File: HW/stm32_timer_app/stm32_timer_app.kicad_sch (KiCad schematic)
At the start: 62 parts, among them J1 105164-0001, J2 61300411121, J3 61300411121, J4 691213710002, J5 691213710002, U1 RT9193-33GB, U2 MOC3041SM, U3 STM32F103C8T6, U4 MAX31865 AMPLIFIER, U5 MMBT2222A-7-F, Y1 ABLS-8.000MHZ-B2-T, Y2 ABS25-32.768KHZ-6-4-T

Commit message: schematic
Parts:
- removed R10: 100K, Resistor_SMD:R_0603_1608Metric, symbol Device:R
- removed R11: 330, Resistor_SMD:R_0603_1608Metric, symbol Device:R
- removed S4: MSS6-V-T_R, MSS6-V-T_R:SW_MSS6-V-T_R, symbol MSS6-V-T_R:MSS6-V-T_R
- removed U3: STM32F103C8T6, STM32F103C8T6:QFP50P900X900X160-48N, symbol STM32F103C8T6:STM32F103C8T6
- removed U4: MAX31865 AMPLIFIER, MAX31865:MAX31865, symbol MAX31865:MAX31865 AMPLIFIER
- removed Y1: ABLS-8.000MHZ-B2-T, ABLS-8.000MHZ-B2-T:XTAL_ABLS-8.000MHZ-B2-T, symbol ABLS-8.000MHZ-B2-T:ABLS-8.000MHZ-B2-T
- removed Y2: ABS25-32.768KHZ-6-4-T, ABS25-32.768KHZ-6-4-T:XTAL_ABS25-32.768KHZ-6-4-T, symbol ABS25-32.768KHZ-6-4-T:ABS25-32.768KHZ-6-4-T
- added C16, C17: 105, LD03ZD475MAB2A:CAPC1608X90, symbol LD03ZD475MAB2A:LD03ZD475MAB2A
- added J4, J5: 61300411121, 61300411121:CONN_61300411121_WRE, symbol 61300411121:61300411121
- added LED1, LED2: 150060GS75000, 150060GS75000:LED_150060GS75000_WRE, symbol 150060GS75000:150060GS75000
- added LED3, LED4: 150060GS75000, LED_150060GS75000_WRE, symbol 150060GS75000:150060GS75000
- added R19: 100K, Resistor_SMD:R_0603_1608Metric, symbol Device:R
- added R20, R21, R22, R4, R6, R8, R9: 330, Resistor_SMD:R_0603_1608Metric, symbol Device:R
- added S2, S5: 1571527-1, 1571527-1:SW_1571527-1, symbol 1571527-1:1571527-1
- added S7, S8: MSS-102559-14A-D, MSS-102559-14A-D:SW_MSS-102559-14A-D, symbol MSS-102559-14A-D:MSS-102559-14A-D
- added U2: STM32F103C8T6, STM32F103C8T6:QFP50P900X900X160-48N, symbol STM32F103C8T6:STM32F103C8T6
- added U3: MAX31865 AMPLIFIER, MAX31865:MAX31865, symbol MAX31865:MAX31865 AMPLIFIER
- added Y1: ABM3-8.000MHZ-J4Q-T, ABM3_8_000MHZ_J4Q_T:XTAL_ABM3-8.000MHZ-J4Q-T, symbol ABM3-8.000MHZ-J4Q-T:ABM3-8.000MHZ-J4Q-T
- added Y2: ABS07-32.768KHZ-T, ABS07-32.768KHZ-T:XTAL_ABS07-32.768KHZ-T, symbol ABS07-32.768KHZ-T:ABS07-32.768KHZ-T
- LED5: renamed from LED1; footprint LED_150060GS75000_WRE -> 150060GS75000:LED_150060GS75000_WRE
- LED6: renamed from LED2; footprint LED_150060GS75000_WRE -> 150060GS75000:LED_150060GS75000_WRE
- renumbered C13 to C1, C3 to C10, C4 to C11, C5 to C12, C1 to C13, C2 to C14, C7 to C15, C12 to C2, C6 to C20, C8 to C3, C9 to C4, C16 to C5, C10 to C6, C15 to C7, C14 to C8, C11 to C9, J4 to J1, J3 to J2, J5 to J3, J2 to J6, J1 to J7, MT3 to MT1, R9 to R1, R7 to R10, R8 to R11, R15 to R12, R14 to R13, R13 to R14, R21 to R15, R20 to R16, R19 to R17, R16 to R18, R25 to R2, R12 to R23, R4 to R24, R1 to R25, R2 to R26, R3 to R27, R26 to R3, R29 to R5, R27 to R7, S1 to S4, S2 to S6, U2 to U1, U1 to U4
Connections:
- net +3.3V: now also DS1.2 (VCC), LS1.P, J4.1, J5.1, LED1.2, LED2.2, R20.2, R21.2, R22.2, S7.2, S8.2, U2.24 (VDD), U2.36 (VDD), U2.48 (VDD), U2.9 (VDDA), U3.1 (VIN)
- net BOOT0: now also U2.44 (BOOT0)
- net BOOT1: now also R19.2, U2.20 (PB2)
- net OSCIN: now also U2.5 (PD0_OSC_IN), Y1.1
- net OSCOUT: now also U2.6 (PD1_OSC_OUT), Y1.2
- net PA0: now also U2.10 (PA0_WKUP); no longer MT2.A, R16.1
- net PA1: now also U2.11 (PA1); no longer MT2.B, R15.1
- net PA11: now also U2.32 (PA11)
- net PA12: now also U2.33 (PA12)
- net PA2: now also U2.12 (PA2); no longer MT2.2, R17.1
- net PA3: now also U2.13 (PA3)
- net PA4: now also R22.1, S5.2, S5.4, U2.14 (PA4); no longer S3.2, S3.4
- net PA5: now also DS1.3 (SCK), U2.15 (PA5)
- net PA6: now also DS1.5 (RES), U2.16 (PA6)
- net PA7: now also DS1.4 (SDA), U2.17 (PA7)
- net PB7: now also J4.4, U2.43 (PB7); no longer J2.4, R2.1
- net PC13: now also U2.2 (PC13-TAMPER-RTC)
- net PC14: now also U2.3 (PC14-OSC32_IN), Y2.1
- net PC15: now also U2.4 (PC15-OSC32_OUT), Y2.2
- net RESET: now also U2.7 (NRST)
- net SWDCLK: now also U2.37 (PA14)
- net SWDIO: now also U2.34 (PA13)
- net PB1: now reaches U5.1 (B)
- net PB1: now also U2.19 (PB1)
- net at U5.3 (C): now also LS1.N
- net +3.3VT: now reaches J2.1
- net +3.3VT: now also LED3.2, LED4.2
- net PA10T: now reaches J2.3
- net PA10T: now also R8.1
- net PB3: now reaches DS1.6 (DC)
- net PB3: now also U2.39 (PB3)
- net PB6: now reaches DS1.7 (CS)
- net PB6: now also U2.42 (PB6)
- net at R18.1: now also S7.1
- new net: J2.4, R2.1
- new net: LED1.1, R4.2
- new net: LED2.1, R6.2
- new net: LED4.1, R9.2
- new net: S5.1, S5.3
- new net: R19.1, S8.1
- new net: LED3.1, R8.2
- new net: S2.1, S2.3
- new net: U2.23 (VSS), U2.35 (VSS), U2.47 (VSS), U2.8 (VSSA)
- new net PA10: J4.3, U2.31 (PA10)
- new net PA15: J5.3, U2.38 (PA15)
- new net PA8: C16.1, R20.1, S2.2, S2.4, U2.29 (PA8)
- new net PA9: C17.1, R21.1, S3.2, S3.4, U2.30 (PA9)
- new net PB0: MT2.2, R17.1, U2.18 (PB0)
- new net PB10: J5.4, U2.21 (PB10)
- new net PB11: U2.22 (PB11), U3.8 (RDY)
- new net PB12: U2.25 (PB12), U3.7 (CS)
- new net PB13: U2.26 (PB13), U3.4 (CLK)
- new net PB14: U2.27 (PB14), U3.6 (SDI)
- new net PB15: U2.28 (PB15), U3.5 (SDO)
- new net PB4: MT2.B, R15.1, U2.40 (PB4)
- new net PB5: MT2.A, R16.1, U2.41 (PB5)
- new net PB8: R4.1, U2.45 (PB8)
- new net PB9: R6.1, U2.46 (PB9)
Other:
- note added: "BUZZER"
- note added: "LEFT OVER PINs"
- note added: "MAX31865 AMPLIFIER"
- note added: "TRIAC DRIVE CONNECTOR"
- moved on the sheet: C1, C10, C11, C12, C13, C14, C15, C19, C2, C20, C3, C4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

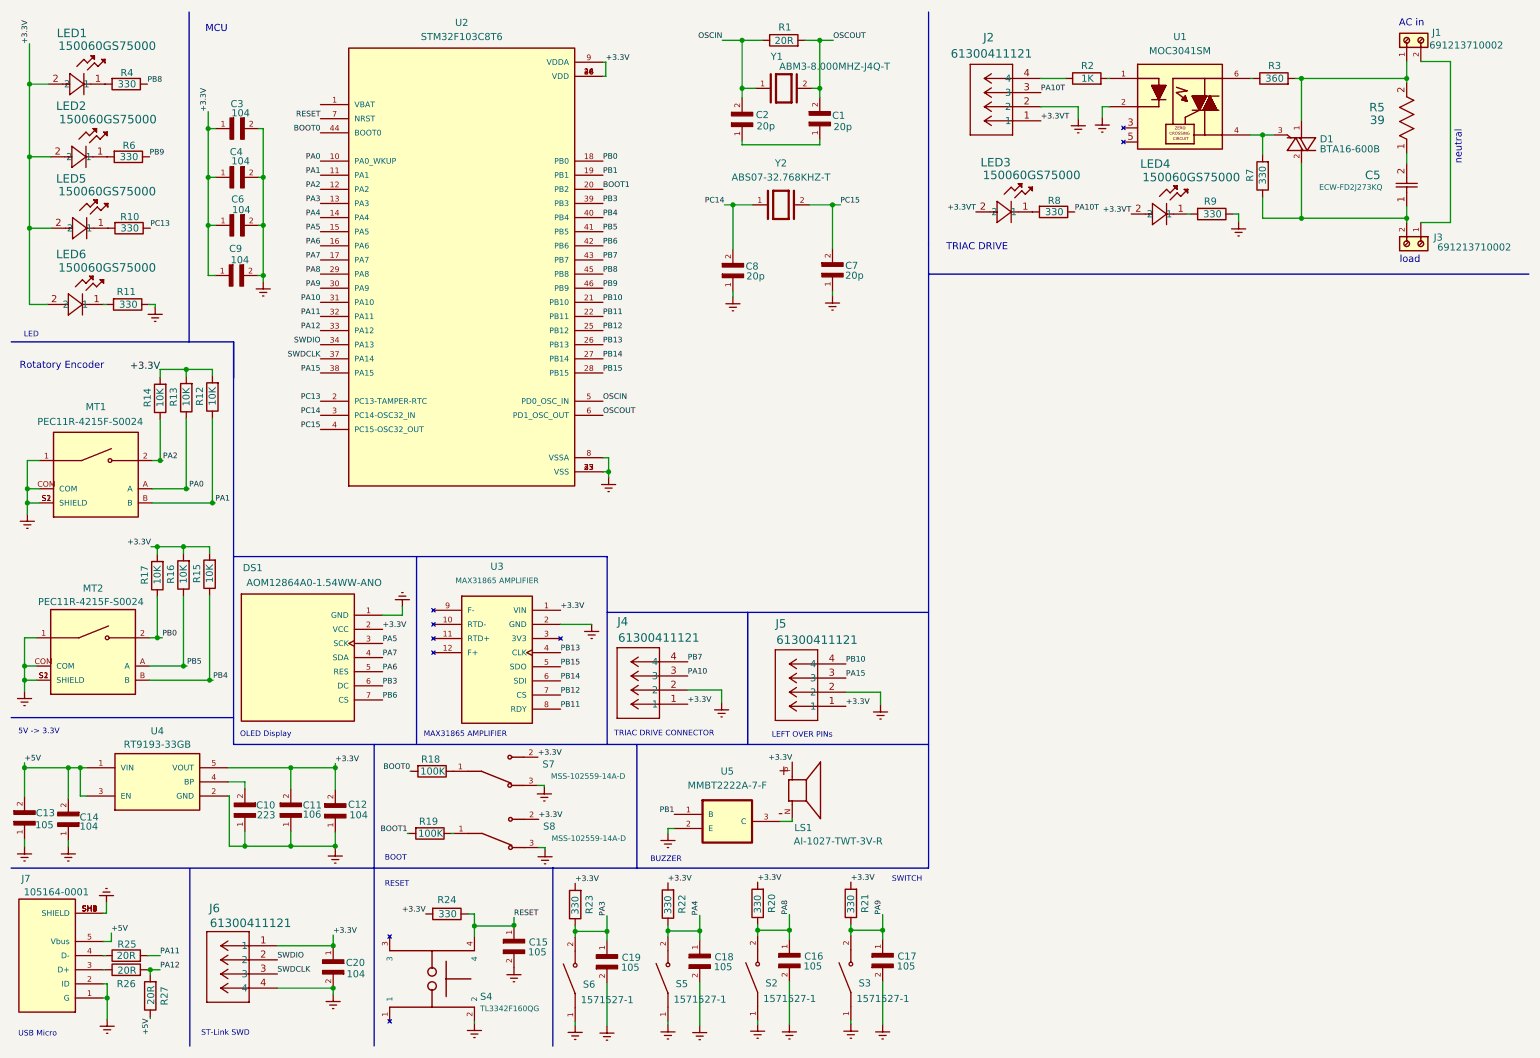
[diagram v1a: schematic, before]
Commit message: schematic update
mcu changed
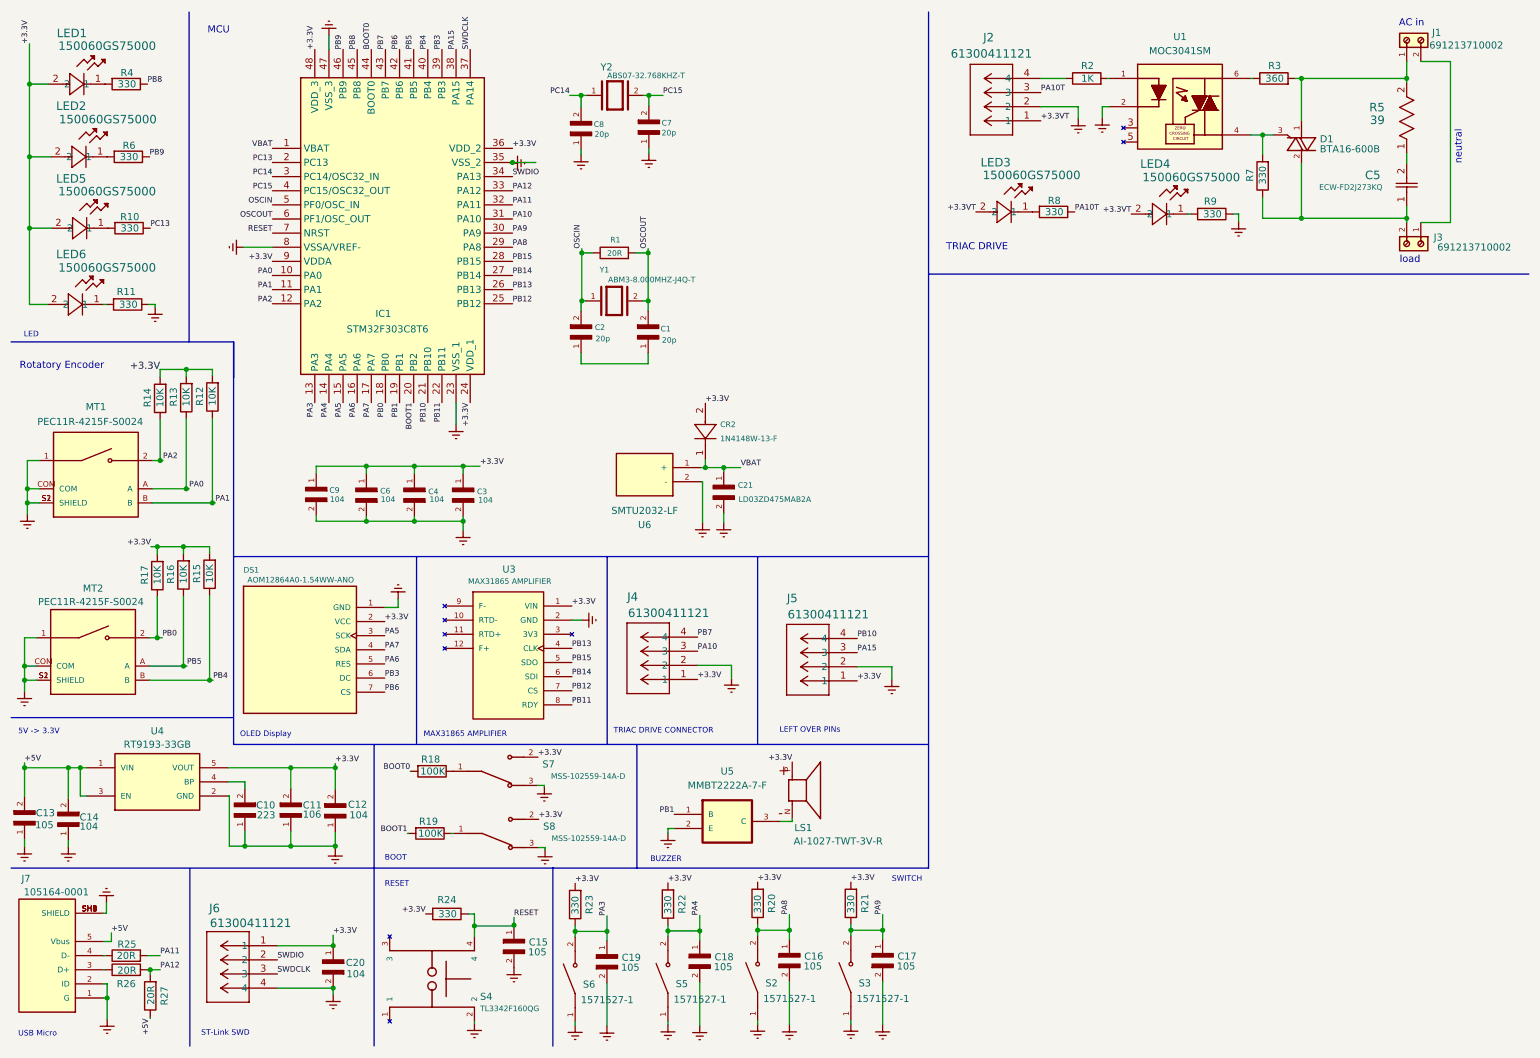
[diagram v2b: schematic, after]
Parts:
- removed U2: STM32F103C8T6, STM32F103C8T6:QFP50P900X900X160-48N, symbol STM32F103C8T6:STM32F103C8T6
- added C21: LD03ZD475MAB2A, LD03ZD475MAB2A:CAPC1608X90, symbol LD03ZD475MAB2A:LD03ZD475MAB2A
- added CR2: 1N4148W-13-F, SOD123_DIO, symbol 1N4148W_13_F:1N4148W-13-F
- added IC1: STM32F303C8T6, QFP50P900X900X160-48N, symbol STM32F303C8T6:STM32F303C8T6
- added U6: SMTU2032-LF, SMTU2032-LF:SMTU2032LF, symbol SMTU2032-LF:SMTU2032-LF
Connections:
- net +3.3V: now also CR2.2, IC1.24 (VDD_1), IC1.36 (VDD_2), IC1.48 (VDD_3), IC1.9 (VDDA)
- net BOOT0: now also IC1.44 (BOOT0)
- net BOOT1: now also IC1.20 (PB2)
- net OSCIN: now also IC1.5 (PF0/OSC_IN)
- net OSCOUT: now also IC1.6 (PF1/OSC_OUT)
- net PA0: now also IC1.10 (PA0)
- net PA1: now also IC1.11 (PA1)
- net PA10: now also IC1.31 (PA10)
- net PA11: now also IC1.32 (PA11)
- net PA12: now also IC1.33 (PA12)
- net PA15: now also IC1.38 (PA15)
- net PA2: now also IC1.12 (PA2)
- net PA3: now also IC1.13 (PA3)
- net PA4: now also IC1.14 (PA4)
- net PA5: now also IC1.15 (PA5)
- net PA6: now also IC1.16 (PA6)
- net PA7: now also IC1.17 (PA7)
- net PA8: now also IC1.29 (PA8)
- net PA9: now also IC1.30 (PA9)
- net PB0: now also IC1.18 (PB0)
- net PB1: now also IC1.19 (PB1)
- net PB10: now also IC1.21 (PB10)
- net PB11: now also IC1.22 (PB11)
- net PB12: now also IC1.25 (PB12)
- net PB13: now also IC1.26 (PB13)
- net PB14: now also IC1.27 (PB14)
- net PB15: now also IC1.28 (PB15)
- net PB3: now also IC1.39 (PB3)
- net PB4: now also IC1.40 (PB4)
- net PB5: now also IC1.41 (PB5)
- net PB6: now also IC1.42 (PB6)
- net PB7: now also IC1.43 (PB7)
- net PB8: now also IC1.45 (PB8)
- net PB9: now also IC1.46 (PB9)
- net PC13: now also IC1.2 (PC13)
- net PC14: now also IC1.3 (PC14/OSC32_IN)
- net PC15: now also IC1.4 (PC15/OSC32_OUT)
- net RESET: now also IC1.7 (NRST)
- net SWDCLK: now also IC1.37 (PA14)
- net SWDIO: now also IC1.34 (PA13)
- new net VBAT: C21.1, CR2.1, IC1.1 (VBAT), U6.1 (+)
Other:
- moved on the sheet: C1, C2, C3, C4, C6, C7, C8, C9, DS1, J4, J5, R1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

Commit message: final schematic
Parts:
- removed C16, C17: 105, LD03ZD475MAB2A:CAPC1608X90, symbol LD03ZD475MAB2A:LD03ZD475MAB2A
- removed IC1: STM32F303C8T6, QFP50P900X900X160-48N, symbol STM32F303C8T6:STM32F303C8T6
- removed J5, J6: 61300411121, 61300411121:CONN_61300411121_WRE, symbol 61300411121:61300411121
- removed R2: 1K, Resistor_SMD:R_0603_1608Metric, symbol Device:R
- removed R20, R21, R7, R8, R9: 330, Resistor_SMD:R_0603_1608Metric, symbol Device:R
- removed R3: 360, Resistor_SMD:R_0603_1608Metric, symbol Device:R
- removed S2, S3: 1571527-1, 1571527-1:SW_1571527-1, symbol 1571527-1:1571527-1
- added C22, C24: 103, LD03ZD475MAB2A:CAPC1608X90, symbol LD03ZD475MAB2A:LD03ZD475MAB2A
- added C23, C25: 104, LD03ZD475MAB2A:CAPC1608X90, symbol LD03ZD475MAB2A:LD03ZD475MAB2A
- added J10: 75160-196-03LF, 75160-196-03LF:AMPHENOL_75160-196-03LF, symbol 75160-196-03LF:75160-196-03LF
- added J5: 54101-G0502LF, 54101-G0502LF:AMPHENOL_54101-G0502LF, symbol 54101-G0502LF:54101-G0502LF
- added J8: PH1RB-04-UA, HDRRA4W64P0X254_1X4_1016X250X850P, symbol PH1RB-04-UA:PH1RB-04-UA
- added J9: PH1RB-05-UA_TEMP., HDRRA5W64P0X254_1X5_1270X250X288P, symbol PH1RB-05-UA_TEMP_:PH1RB-05-UA_TEMP.
- added R2, R20, R7, R9: 330, RC1206N_YAG, symbol 2024-01-02_23-39-38:RC1206FR-0728RL
- added R8: 1k, RC1206N_YAG, symbol 2024-01-02_23-39-38:RC1206FR-0728RL
- added TP1, TP11, TP12, TP13, TP14, TP15, TP16, TP17, TP19, TP2, TP20, TP21, TP22, TP23, TP25, TP4, TP5, TP8: TestPoint_Probe, TestPoint:TestPoint_THTPad_D2.0mm_Drill1.0mm, symbol Connector:TestPoint_Probe
- added U2: STM32F303C8T6, QFP50P900X900X160-48N, symbol STM32F303C8T6:STM32F303C8T6
- added U8: MPU-6050, QFN24_4X4X0P9_IVS, symbol MPU_6050:MPU-6050
- LED1, LED2: footprint 150060GS75000:LED_150060GS75000_WRE -> LED_150060GS75000_WRE
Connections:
- net PB13 is gone; now on net PA5: U3.4 (CLK)
- net +3.3V: now also J4.2, C22.2, C25.1, J8.2, J9.5, TP17.1, U2.24 (VDD_1), U2.36 (VDD_2), U2.48 (VDD_3), U2.9 (VDDA), U8.13 (VDD), U8.8 (VLOGIC); no longer J4.1
- net +3.3VT: now also J2.2; no longer J2.1
- net +5V: now also J10.3, TP1.1
- net BOOT0: now also U2.44 (BOOT0)
- net BOOT1: now also U2.20 (PB2)
- net OSCIN: now also TP14.1, U2.5 (PF0/OSC_IN)
- net OSCOUT: now also TP13.1, U2.6 (PF1/OSC_OUT)
- net PA0: now also MT1.B, R12.1, TP19.1, U2.10 (PA0); no longer MT1.A, R13.1
- net PA1: now also MT1.A, R13.1, TP20.1, U2.11 (PA1); no longer MT1.B, R12.1
- net PA10: now also J10.2, U2.31 (PA10); no longer J4.3
- net PA11: now also TP25.1, U2.32 (PA11)
- net PA12: now also TP2.1, U2.33 (PA12)
- net PA15: now also U2.38 (PA15), U8.23 (SCL)
- net PA2: now also C19.1, R23.1, S6.2, S6.4, U2.12 (PA2); no longer MT1.2, R14.1
- net PA3: now also MT1.2, R14.1, TP21.1, U2.13 (PA3); no longer C19.1, R23.1, S6.2, S6.4
- net PA4: now also MT2.A, R16.1, TP22.1, U2.14 (PA4); no longer C18.1, R22.1, S5.2, S5.4
- net PA5: now also U2.15 (PA5)
- net PA6: now also U3.6 (SDI), U2.16 (PA6); no longer DS1.5 (RES)
- net PA7: now also U3.5 (SDO), U2.17 (PA7)
- net PA8: now also U2.29 (PA8), U8.12 (INT)
- net PA9: now also J8.4, U2.30 (PA9)
- net PB0: now also TP23.1, U2.18 (PB0)
- net PB1: now also TP4.1, U2.19 (PB1)
- net PB10: now also J8.3, U2.21 (PB10)
- net PB11: now also U2.22 (PB11)
- net PB12: now also R4.1, U2.25 (PB12); no longer U3.7 (CS)
- net PB14: now also J4.3, U2.27 (PB14); no longer U3.6 (SDI)
- net PB15: now also J4.4, U2.28 (PB15); no longer U3.5 (SDO)
- net PB3: now also J9.4, U2.39 (PB3); no longer DS1.6 (DC)
- net PB4: now also TP8.1, U2.40 (PB4)
- net PB5: now also DS1.6 (DC), U2.41 (PB5); no longer MT2.A, R16.1
- net PB6: now also U3.7 (CS), U2.42 (PB6)
- net PB7: now also U2.43 (PB7), U8.24 (SDA); no longer J4.4
- net PB8: now also DS1.5 (RES), U2.45 (PB8); no longer R4.1
- net PB9: now also U2.46 (PB9)
- net PC13: now also U2.2 (PC13)
- net PC14: now also TP16.1, U2.3 (PC14/OSC32_IN)
- net PC15: now also TP15.1, U2.4 (PC15/OSC32_OUT)
- net RESET: now also U2.7 (NRST)
- net SWDCLK: now also J9.2, U2.37 (PA14)
- net SWDIO: now also J9.3, U2.34 (PA13)
- net VBAT: now also TP11.1, U2.1 (VBAT)
- net GND: now reaches C10.1, C11.1, C12.1, U4.2 (GND)
- net GND: now also C1.1, C13.1, C14.1, C15.2, C18.2, C19.2, C2.1, C20.2, C21.2, C3.2, C4.2, C6.2, C7.1, C8.1, C9.2, DS1.1 (GND), J2.1, J4.1, J7.1 (G), J7.2 (ID), J7.SH1 (SHIELD), J7.SH2 (SHIELD), J7.SH3 (SHIELD), J7.SH4 (SHIELD), J7.SH5 (SHIELD), J7.SH6 (SHIELD), MT1.1, MT1.COM, MT1.S1 (SHIELD), MT1.S2 (SHIELD), MT2.1, MT2.COM, MT2.S1 (SHIELD), MT2.S2 (SHIELD), R11.1, S4.2, S5.1, S5.3, S6.1, S6.3, S7.3, S8.3, U1.2, U3.2 (GND), U5.2 (E), U6.2 (-), C22.1, C25.2, J10.1, J8.1, J9.1, R20.1, TP12.1, U2.23 (VSS_1), U2.35 (VSS_2), U2.47 (VSS_3), U2.8 (VSSA/VREF-), U8.1 (CLKIN), U8.9 (AD0)
- net at D1.1, J1.1, R5.2: now also R7.1
- net at U1.1: now also R8.1
- net at D1.3, U1.4: now also R2.1
- net at U1.6: now also R7.2
- net at J2.4: now also R8.2
- net at LED1.1: now also R6.2; no longer R4.2
- net at LED2.1: now also R4.2; no longer R6.2
- net at C5.1, D1.2, J3.2: now also R2.2
- net at LS1.N, U5.3 (C): now also TP5.1
- net at LED4.1: now also R20.2
- net at LED3.1: now also R9.2
- net PA10T renamed LED
- net LED: now also R9.1
- new net: C23.1, U8.10 (REGOUT)
- new net: C23.2, U8.11 (FSYNC)
- new net: C24.2, U8.18 (GND)
- new net: C24.1, U8.20 (CPOUT)
- new net AUX_CL: J5.A2, U8.7 (AUX_CL)
- new net AUX_DA: J5.A1, U8.6 (AUX_DA)
- new net PA13: C18.1, R22.1, S5.2, S5.4, U2.26 (PB13)
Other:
- note added: "CAPACITIVE TOUCH"
- note added: "MPU6050 6DOF ACC+GYRO SENSOR"
- note added: "USART1"
- note removed: "LEFT OVER PINs"
- company: (none) -> NC
- title: (none) -> STM32_Timer_APP
- moved on the sheet: C1, C15, C18, C19, C2, C20, C21, C7, C8, CR2, J2, LED3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
